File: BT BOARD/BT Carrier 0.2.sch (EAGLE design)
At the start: 3 parts, among them M1 RN4020

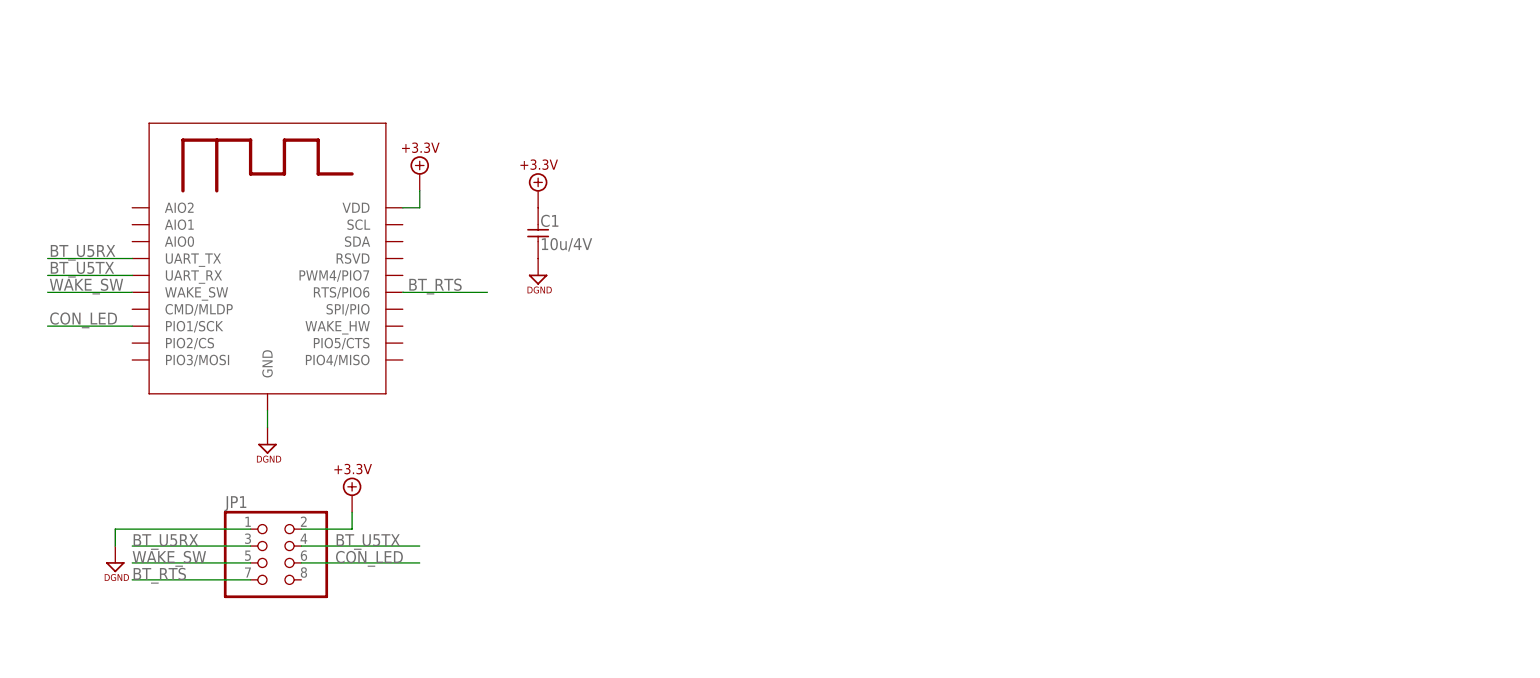
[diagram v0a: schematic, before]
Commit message: added connector board
added connector board and routed. found allignment issue in BT board, and fixed it, need to get files approved by Petr and Jaroslav.
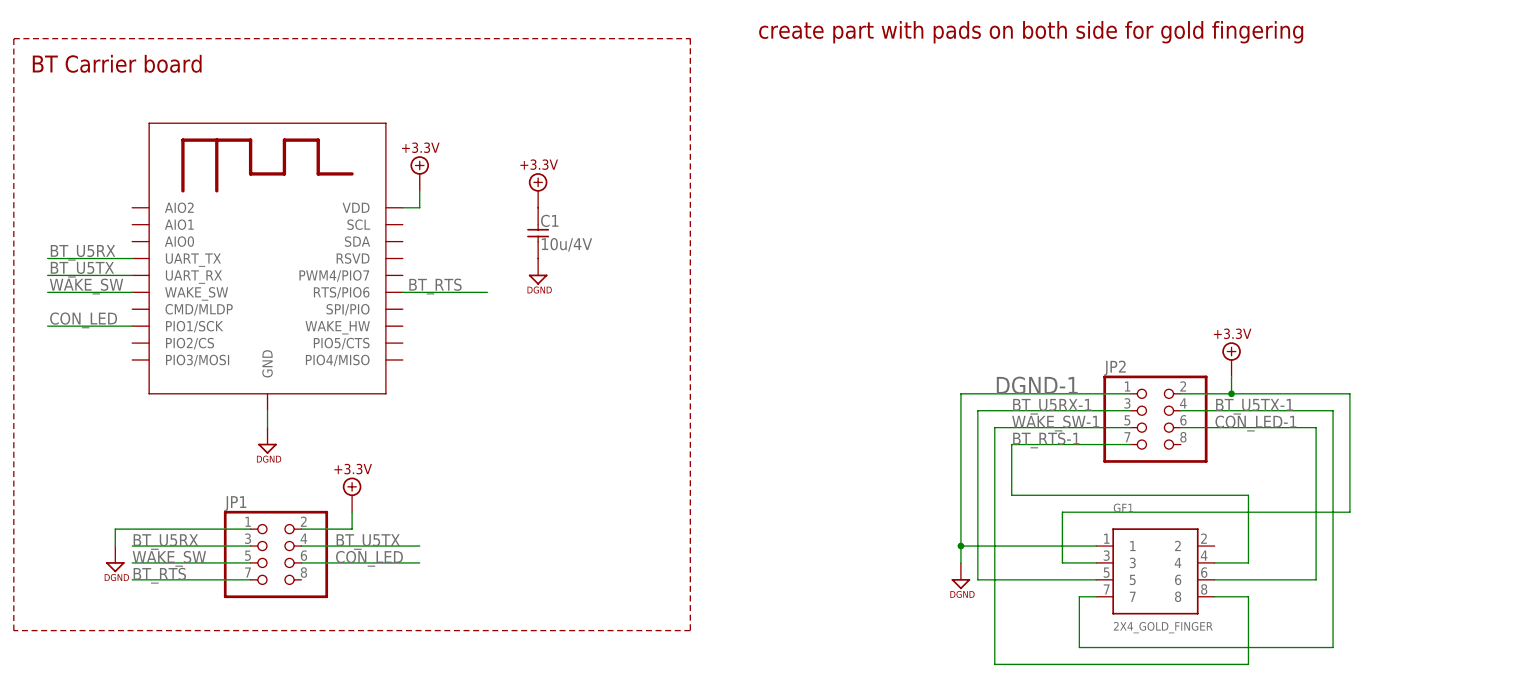
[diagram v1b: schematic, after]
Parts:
- added GF1: 2X4_GOLD_FINGER, clackboard_lib:2X4_GOLD_FINGER
- added JP2: (no value), pinhead:PINHD-2X4
- C1: device DISCRETE:C-0603 -> discrete:C-0603
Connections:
- new net +3.3V-1: GF1.3, JP2.2
- new net BT_RTS-1: GF1.4, JP2.7
- new net BT_U5RX-1: GF1.5, JP2.3
- new net BT_U5TX-1: GF1.7, JP2.4
- new net CON_LED-1: GF1.6, JP2.6
- new net DGND-1: GF1.1, JP2.1
- new net WAKE_SW-1: GF1.8, JP2.5
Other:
- note added: "BT Carrier board"
- note added: "create part with pads on both side for gold fingering"
